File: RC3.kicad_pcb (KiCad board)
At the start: 2 copper layers, 84.8 x 91.4 mm, 46 parts, among them P1 CONN_2, P2 CONN_3, P3 CONN_3X2, P4 CONN_2, Q1 MOSFET_N, Q10 MOSFET_N, Q11 MOSFET_N, Q12 MOSFET_N, Q13 MOSFET_N, Q14 MOSFET_N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

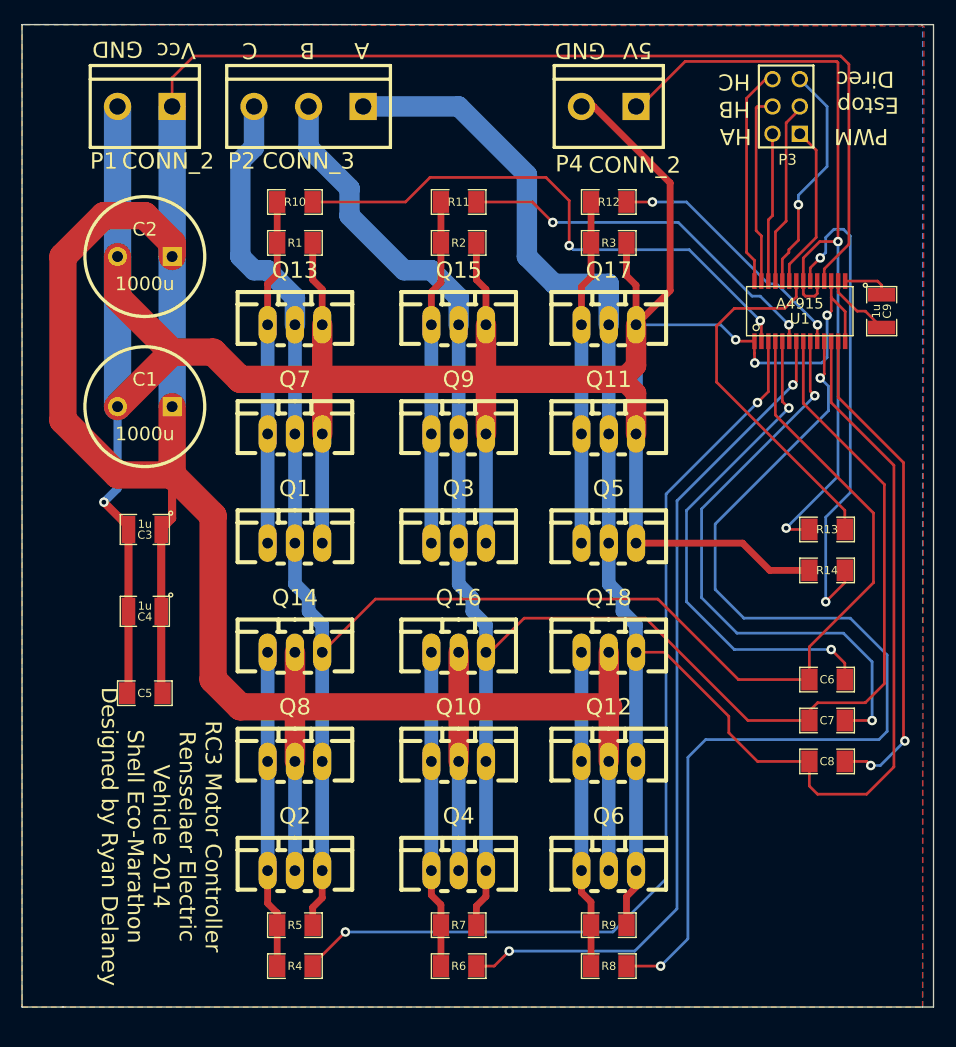
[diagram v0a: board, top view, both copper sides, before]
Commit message: Added flyback diodes and heatskinks
All legs of the motor controller now have flyback diodes and FETs are
now arranged in a manner that heat sinks can be applied. All inputs also
have pull-down resistors and the 5 VDC has filtering capacitors
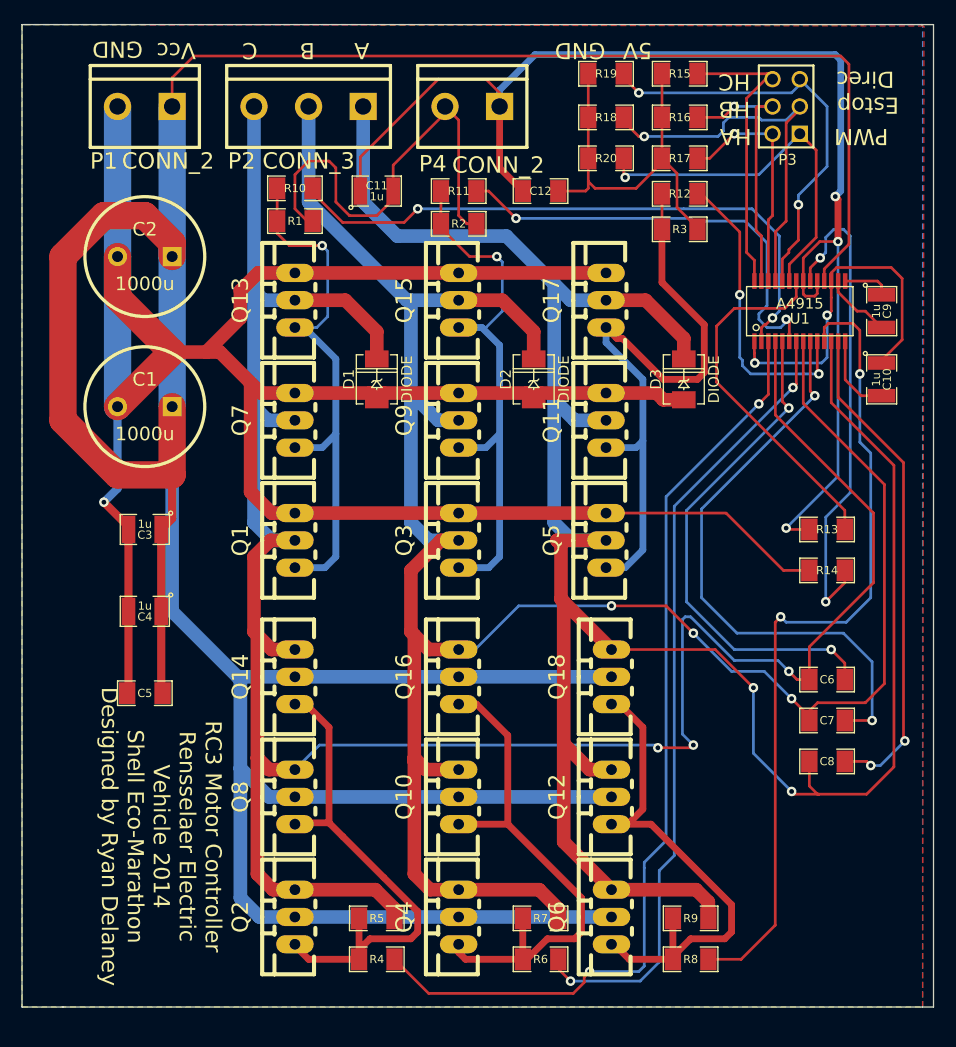
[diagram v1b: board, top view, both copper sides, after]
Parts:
- added C10: 1u, SM1210, F.Cu at (222.2, 168.9)
- added C11: 1u, SM1210, F.Cu at (175.3, 151.4)
- added C12: 47n, SM1206, F.Cu at (190.5, 151.4)
- added D1: DIODE, DO-214AC(SMA), F.Cu at (175.3, 168.9)
- added D2: DIODE, DO-214AC(SMA), F.Cu at (189.9, 168.9)
- added D3: DIODE, DO-214AC(SMA), F.Cu at (203.8, 168.9)
- added R15: 10K, SM1206, F.Cu at (203.5, 140.5)
- added R16: 10K, SM1206, F.Cu at (203.5, 144.5)
- added R17: 10K, SM1206, F.Cu at (203.5, 148.3)
- added R18: 10K, SM1206, F.Cu at (196.6, 144.5)
- added R19: 10K, SM1206, F.Cu at (196.6, 140.5)
- added R20: 10K, SM1206, F.Cu at (196.6, 148.3)
- moved P4 12.7 mm to (184.2, 143.5)
- moved R4 7.65 mm to (175.3, 222.9)
- moved R5 7.65 mm to (175.3, 219.1)
- moved R6 7.65 mm to (190.5, 222.9)
- moved R7 7.65 mm to (190.5, 219.1)
- moved R8 7.65 mm to (204.5, 222.9)
- moved R9 7.65 mm to (204.5, 219.1)
- moved R3 6.73 mm to (203.5, 154.9)
- moved R12 6.65 mm to (203.5, 151.6)
- moved Q6 4.33 mm to (197.1, 218.9), turned to 90 degrees
- moved Q2 4.32 mm to (167.6, 218.9), turned to 90 degrees
- moved Q4 4.32 mm to (182.9, 218.9), turned to 90 degrees
- moved Q12 3.31 mm to (197.1, 207.8), turned to 90 degrees
- moved Q10 3.30 mm to (182.9, 207.8), turned to 90 degrees
- moved Q8 3.30 mm to (167.6, 207.8), turned to 90 degrees
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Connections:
- U1 pad 14: GND -> N-0000011
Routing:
- net OUT_C: track 169.2 -> 223.6 mm, vias 0 -> 3
- net OUT_A: track 170.1 -> 223.2 mm, vias 0 -> 2
- net OUT_B: track 164.2 -> 210.8 mm, vias 0 -> 3
- net +5V: track 78.0 -> 122.5 mm, vias 2 -> 3
- net GND: track 309.1 -> 345.4 mm, vias 4 -> 3
- net N-000009: track 32.1 -> 59.6 mm
- net N-0000017: track 96.8 -> 76.3 mm
- net PWM: track 15.4 -> 35.1 mm, vias 0 -> 1
- net N-000001: track 29.6 -> 48.8 mm
- net ESTOPn: track 17.2 -> 36.4 mm, vias 0 -> 1
- net N-0000014: track 32.1 -> 51.1 mm, vias 0 -> 1
- net N-000008: track 29.6 -> 48.5 mm
- net N-000004: track 32.1 -> 50.3 mm, vias 0 -> 1
- net DIREC: track 21.6 -> 39.7 mm, vias 1 -> 2
- net N-0000015: track 29.6 -> 47.2 mm
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
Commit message: Modified PCB to have mounting holes and keep out
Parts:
- added 1PIN: P***, 1pin, F.Cu at (146.7, 222.9)
- added 1PIN: P***, 1pin, F.Cu at (221.6, 222.2)
- added 1PIN: P***, 1pin, F.Cu at (222.2, 139.7)
- added ?: P***, 1PIN_SMD, F.Cu at (215.4, 162.7)
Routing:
- net +48V: track 338.6 -> 319.8 mm
- net GND: track 345.4 -> 359.8 mm
- removed copper zone on F.Cu, net GND
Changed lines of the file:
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@@
   (general
     (links 133)
-    (no_connects 0)
-    (area 142.189999 135.839999 227.126001 227.380001)
+    (no_connects 1)
+    (area 140.008286 135.839999 227.126001 227.380001)
     (thickness 1.6)
-    (drawings 22)
-    (tracks 625)
+    (drawings 23)
+    (tracks 627)
     (zones 0)
-    (modules 58)
+    (modules 62)
     (nets 33)
   )
@@
     (mod_text_size 1 1)
     (mod_text_width 0.15)
-    (pad_size 1.5 1.5)
-    (pad_drill 0.6)
+    (pad_size 2 2)
+    (pad_drill 0)
     (pad_to_mask_clearance 0)
     (aux_axis_origin 220.599 222.504)
@@
     (uvia_drill 0.127)
   )
+  (module 1PIN_SMD (layer F.Cu)
+    (at 215.392 162.687)
+    (descr "module 1 pin (ou trou mecanique de percage)")
+    (tags DEV)
+    (path 1pin)
+    (zone_connect 1)
+    (fp_text reference "" (at 0 -3.50012) (layer F.SilkS)
+      (effects (font (size 1 1) (thickness 0.15)))
+    )
+    (fp_text value P*** (at 0 2.54) (layer F.SilkS)
+      (effects (font (size 1.016 1.016) (thickness 0.254)))
+    )
+    (pad 1 smd rect (at 0 0) (size 2 2)
+      (layers F.Cu F.SilkS F.Mask)
+      (net 5 GND)
+      (zone_connect 1)
+    )
+  )
   (module tssop-28 (layer F.Cu)
     (at 214.63 162.56)
@@
     )
   )
+  (module 1pin (layer F.Cu)
+    (at 146.685 222.885)
+    (descr "module 1 pin (ou trou mecanique de percage)")
+    (tags DEV)
+    (path 1pin)
+    (fp_text reference 1PIN (at 0 -3.048) (layer F.SilkS)
+      (effects (font (size 1.016 1.016) (thickness 0.254)))
+    )
+    (fp_text value P*** (at 0 2.794) (layer F.SilkS) hide
+      (effects (font (size 1.016 1.016) (thickness 0.254)))
+    )
+    (fp_circle (center 0 0) (end 0 -2.286) (layer F.SilkS) (width 0.381))
+    (pad 1 thru_hole circle (at 0 0) (size 4.064 4.064) (drill 3.048)
+      (layers *.Cu *.Mask F.SilkS)
+    )
+  )
+  (module 1pin (layer F.Cu)
+    (at 221.615 222.25)
+    (descr "module 1 pin (ou trou mecanique de percage)")
+    (tags DEV)
+    (path 1pin)
+    (fp_text reference 1PIN (at 0 -3.048) (layer F.SilkS)
+      (effects (font (size 1.016 1.016) (thickness 0.254)))
+    )
+    (fp_text value P*** (at 0 2.794) (layer F.SilkS) hide
+      (effects (font (size 1.016 1.016) (thickness 0.254)))
+    )
+    (fp_circle (center 0 0) (end 0 -2.286) (layer F.SilkS) (width 0.381))
+    (pad 1 thru_hole circle (at 0 0) (size 4.064 4.064) (drill 3.048)
+      (layers *.Cu *.Mask F.SilkS)
+    )
+  )
+  (module 1pin (layer F.Cu)
+    (at 222.25 139.7)
+    (descr "module 1 pin (ou trou mecanique de percage)")
+    (tags DEV)
+    (path 1pin)
+    (fp_text reference 1PIN (at 0 -3.048) (layer F.SilkS)
+      (effects (font (size 1.016 1.016) (thickness 0.254)))
+    )
+    (fp_text value P*** (at 0 2.794) (layer F.SilkS) hide
+      (effects (font (size 1.016 1.016) (thickness 0.254)))
+    )
+    (fp_circle (center 0 0) (end 0 -2.286) (layer F.SilkS) (width 0.381))
+    (pad 1 thru_hole circle (at 0 0) (size 4.064 4.064) (drill 3.048)
+      (layers *.Cu *.Mask F.SilkS)
+    )
+  )
+  (target plus (at 148.59 134.62) (size 0.005) (width 0.1) (layer Edge.Cuts))
   (gr_line (start 227.076 227.33) (end 226.06 227.33) (angle 90) (layer Edge.Cuts) (width 0.1))
   (gr_line (start 227.076 135.89) (end 227.076 227.33) (angle 90) (layer Edge.Cuts) (width 0.1))
@@
   (gr_line (start 226.06 135.89) (end 142.24 135.89) (angle 90) (layer Edge.Cuts) (width 0.1))
   (gr_line (start 146.05 227.33) (end 226.06 227.33) (angle 90) (layer Edge.Cuts) (width 0.1))
+  (segment (start 156.21 157.48) (end 156.21 153.67) (width 2.54) (layer F.Cu) (net 1))
+  (segment (start 156.21 173.99) (end 156.21 171.45) (width 2.54) (layer F.Cu) (net 1))
+  (segment (start 153.67 176.53) (end 156.21 173.99) (width 2.54) (layer F.Cu) (net 1))
+  (segment (start 149.86 176.53) (end 153.67 176.53) (width 2.54) (layer F.Cu) (net 1))
+  (segment (start 146.05 172.72) (end 149.86 176.53) (width 2.54) (layer F.Cu) (net 1))
+  (segment (start 146.05 154.94) (end 146.05 172.72) (width 2.54) (layer F.Cu) (net 1))
+  (segment (start 148.59 152.4) (end 146.05 154.94) (width 2.54) (layer F.Cu) (net 1))
+  (segment (start 154.94 152.4) (end 148.59 152.4) (width 2.54) (layer F.Cu) (net 1))
+  (segment (start 156.21 153.67) (end 154.94 152.4) (width 2.54) (layer F.Cu) (net 1))
   (segment (start 182.88 218.948) (end 197.104 218.948) (width 1.27) (layer B.Cu) (net 1))
   (segment (start 167.64 218.948) (end 182.88 218.948) (width 1.27) (layer B.Cu) (net 1))
@@
   (segment (start 167.64 196.596) (end 182.88 196.596) (width 1.27) (layer B.Cu) (net 1))
   (segment (start 156.21 171.45) (end 156.21 190.5) (width 1.27) (layer B.Cu) (net 1))
+  (segment (start 156.21 190.5) (end 162.306 196.596) (width 1.27) (layer B.Cu) (net 1))
   (segment (start 162.306 196.596) (end 162.56 196.596) (width 1.27) (layer B.Cu) (net 1))
   (segment (start 162.56 196.596) (end 167.64 196.596) (width 1.27) (layer B.Cu) (net 1))
-  (segment (start 156.21 190.5) (end 162.306 196.596) (width 1.27) (layer B.Cu) (net 1))
   (segment (start 216.90584 159.76092) (end 216.90584 158.63316) (width 0.254) (layer F.Cu) (net 1))
   (segment (start 156.21 140.843) (end 156.21 143.51) (width 0.254) (layer F.Cu) (net 1))
@@
   (segment (start 155.194 197.993) (end 155.321 198.12) (width 0.762) (layer F.Cu) (net 1))
   (segment (start 155.194 182.88) (end 155.194 190.5) (width 0.762) (layer F.Cu) (net 1))
-  (segment (start 156.21 177.8) (end 156.21 181.864) (width 0.762) (layer F.Cu) (net 1))
-  (segment (start 156.21 181.864) (end 155.194 182.88) (width 0.762) (layer F.Cu) (net 1))
-  (segment (start 156.21 171.45) (end 156.21 177.8) (width 2.54) (layer F.Cu) (net 1))
-  (segment (start 156.21 157.48) (end 156.21 156.21) (width 2.54) (layer F.Cu) (net 1))
-  (segment (start 156.21 156.21) (end 153.67 153.67) (width 2.54) (layer F.Cu) (net 1))
-  (segment (start 153.67 153.67) (end 149.86 153.67) (width 2.54) (layer F.Cu) (net 1))
-  (segment (start 149.86 153.67) (end 146.05 157.48) (width 2.54) (layer F.Cu) (net 1))
-  (segment (start 146.05 157.48) (end 146.05 172.72) (width 2.54) (layer F.Cu) (net 1))
-  (segment (start 146.05 172.72) (end 151.13 177.8) (width 2.54) (layer F.Cu) (net 1))
-  (segment (start 151.13 177.8) (end 156.21 177.8) (width 2.54) (layer F.Cu) (net 1))
-  (segment (start 156.21 157.48) (end 156.21 171.45) (width 2.54) (layer B.Cu) (net 1))
   (segment (start 156.21 143.51) (end 156.21 157.48) (width 2.54) (layer B.Cu) (net 1))
   (segment (start 218.186 156.083) (end 218.186 152.146) (width 0.635) (layer F.Cu) (net 2))
@@
   (segment (start 213.36 145.034) (end 213.36 154.178) (width 0.254) (layer F.Cu) (net 4))
   (segment (start 214.63 143.764) (end 213.36 145.034) (width 0.254) (layer F.Cu) (net 4))
+  (segment (start 194.945 151.13) (end 194.945 153.035) (width 0.254) (layer F.Cu) (net 5))
+  (segment (start 186.309 156.21) (end 184.531 154.432) (width 0.254) (layer F.Cu) (net 5))
+  (segment (start 191.77 156.21) (end 186.309 156.21) (width 0.254) (layer F.Cu) (net 5))
+  (segment (start 194.945 153.035) (end 191.77 156.21) (width 0.254) (layer F.Cu) (net 5))
   (segment (start 194.945 144.526) (end 194.945 148.336) (width 0.254) (layer F.Cu) (net 5))
   (segment (start 194.945 140.462) (end 194.945 144.526) (width 0.254) (layer F.Cu) (net 5))
@@
   (segment (start 168.783 154.178) (end 167.64 153.035) (width 0.254) (layer F.Cu) (net 5))
   (segment (start 184.531 154.432) (end 183.642 154.432) (width 0.254) (layer F.Cu) (net 5))
-  (segment (start 182.88 144.78) (end 181.61 143.51) (width 0.254) (layer F.Cu) (net 5))
-  (segment (start 182.88 153.67) (end 182.88 144.78) (width 0.254) (layer F.Cu) (net 5))
   (segment (start 183.642 154.432) (end 182.88 153.67) (width 0.254) (layer F.Cu) (net 5))
+  (segment (start 182.88 153.67) (end 182.88 144.78) (width 0.254) (layer F.Cu) (net 5))
+  (segment (start 182.88 144.78) (end 181.61 143.51) (width 0.254) (layer F.Cu) (net 5))
   (segment (start 181.61 143.51) (end 181.61 144.145) (width 0.254) (layer F.Cu) (net 5))
   (segment (start 176.784 148.971) (end 176.784 151.384) (width 0.254) (layer F.Cu) (net 5))
@@
     )
   )
-  (zone (net 5) (net_name GND) (layer F.Cu) (hatch edge 0.508)
+  (zone (net 0) (net_name "") (layer B.Cu) (hatch edge 0.508)
     (connect_pads (clearance 0.508))
     (min_thickness 0.254)
+    (keepout (tracks allowed) (vias allowed) (copperpour not_allowed))
     (fill (arc_segments 16) (thermal_gap 0.508) (thermal_bridge_width 0.508))
     (polygon
       (pts
-        (xy 142.24 135.89) (xy 142.24 227.33) (xy 226.06 227.33) (xy 226.187 136.017)
+        (xy 204.47 224.79) (xy 158.75 224.79) (xy 159.385 156.845) (xy 203.835 156.845)
       )
     )
